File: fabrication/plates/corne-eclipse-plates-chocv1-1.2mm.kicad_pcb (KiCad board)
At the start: 2 copper layers, 272.4 x 180.5 mm, 46 parts

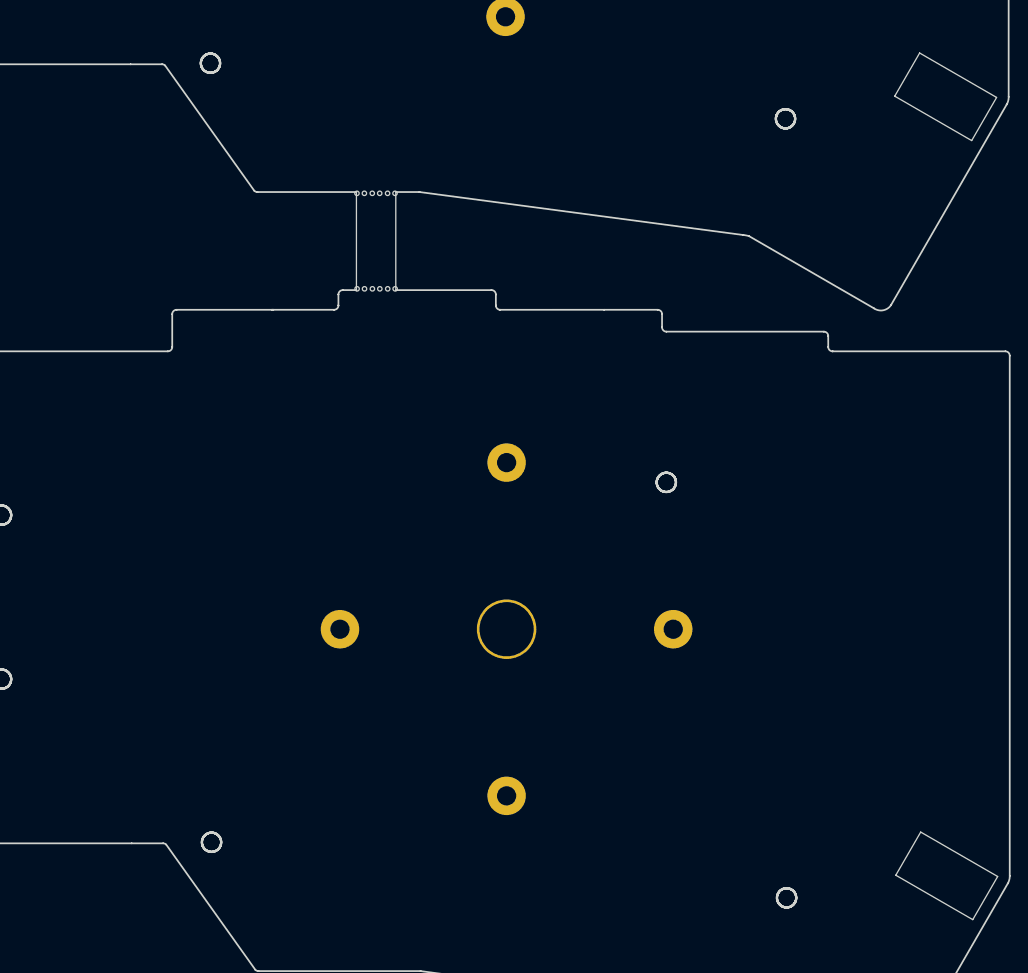
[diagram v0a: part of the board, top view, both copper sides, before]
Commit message: wip: silkscreen, QR codes, plate renames, LED34 cleanup
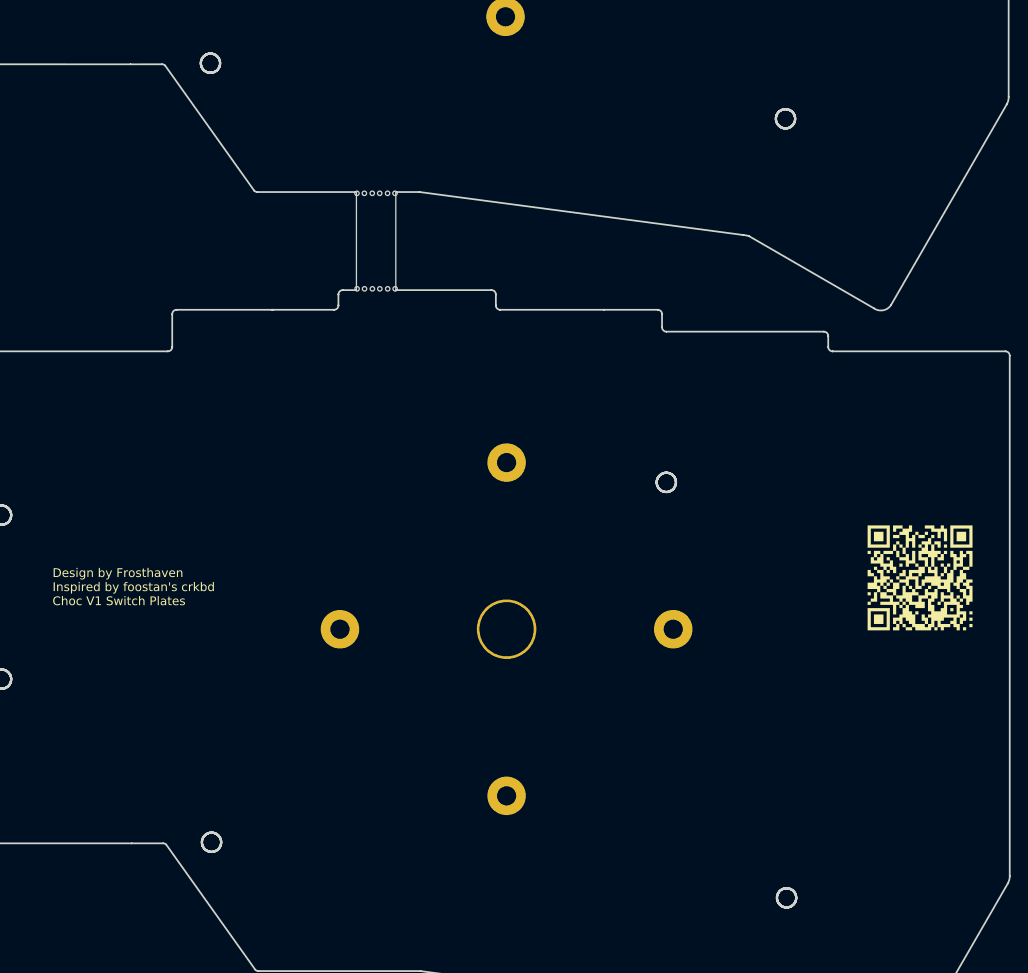
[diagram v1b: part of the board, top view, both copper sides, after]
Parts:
- removed the REF** at (276.5, 174.6)
- removed the REF** at (276.3, 85.6)
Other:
- board text added: "Design by Frosthaven Inspired by foostan's crkbd Choc V1 Switch Plates"

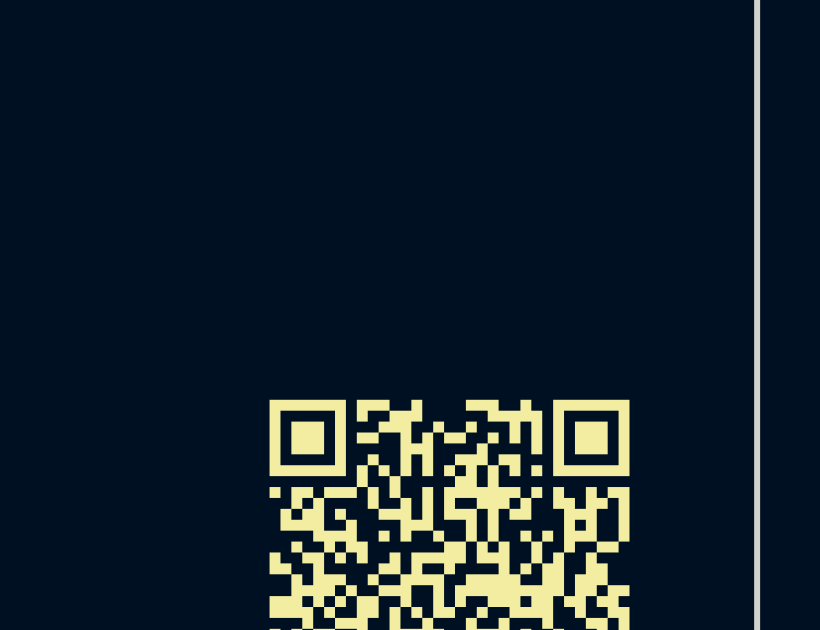
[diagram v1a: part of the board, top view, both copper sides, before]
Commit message: wip: logos, silkscreen cleanup, choc shield STLs, diode alignment
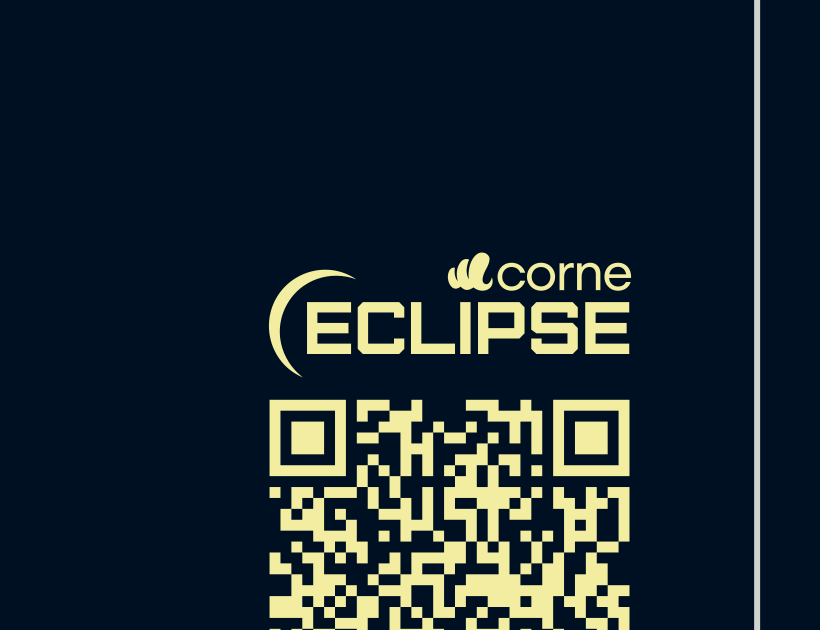
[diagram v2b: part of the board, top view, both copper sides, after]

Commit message: wip
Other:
- outline, holes or cut-outs redrawn

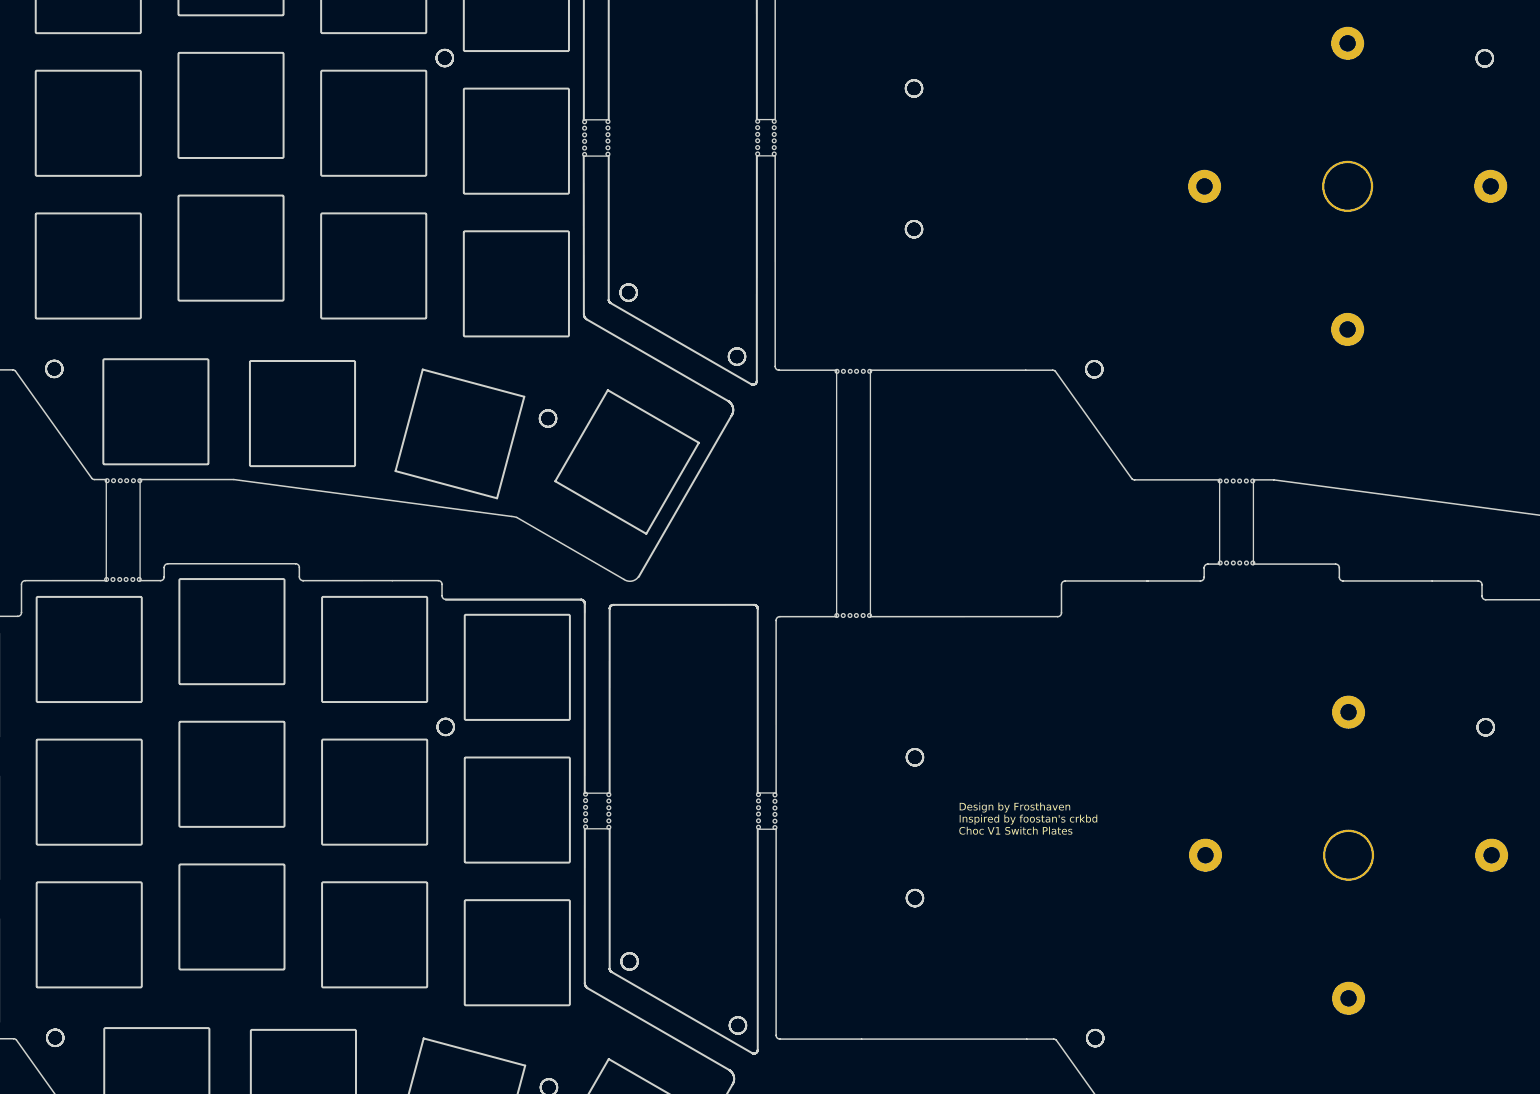
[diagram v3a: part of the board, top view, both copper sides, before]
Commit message: fix(pcbs): aligned screw holes on lp and mx
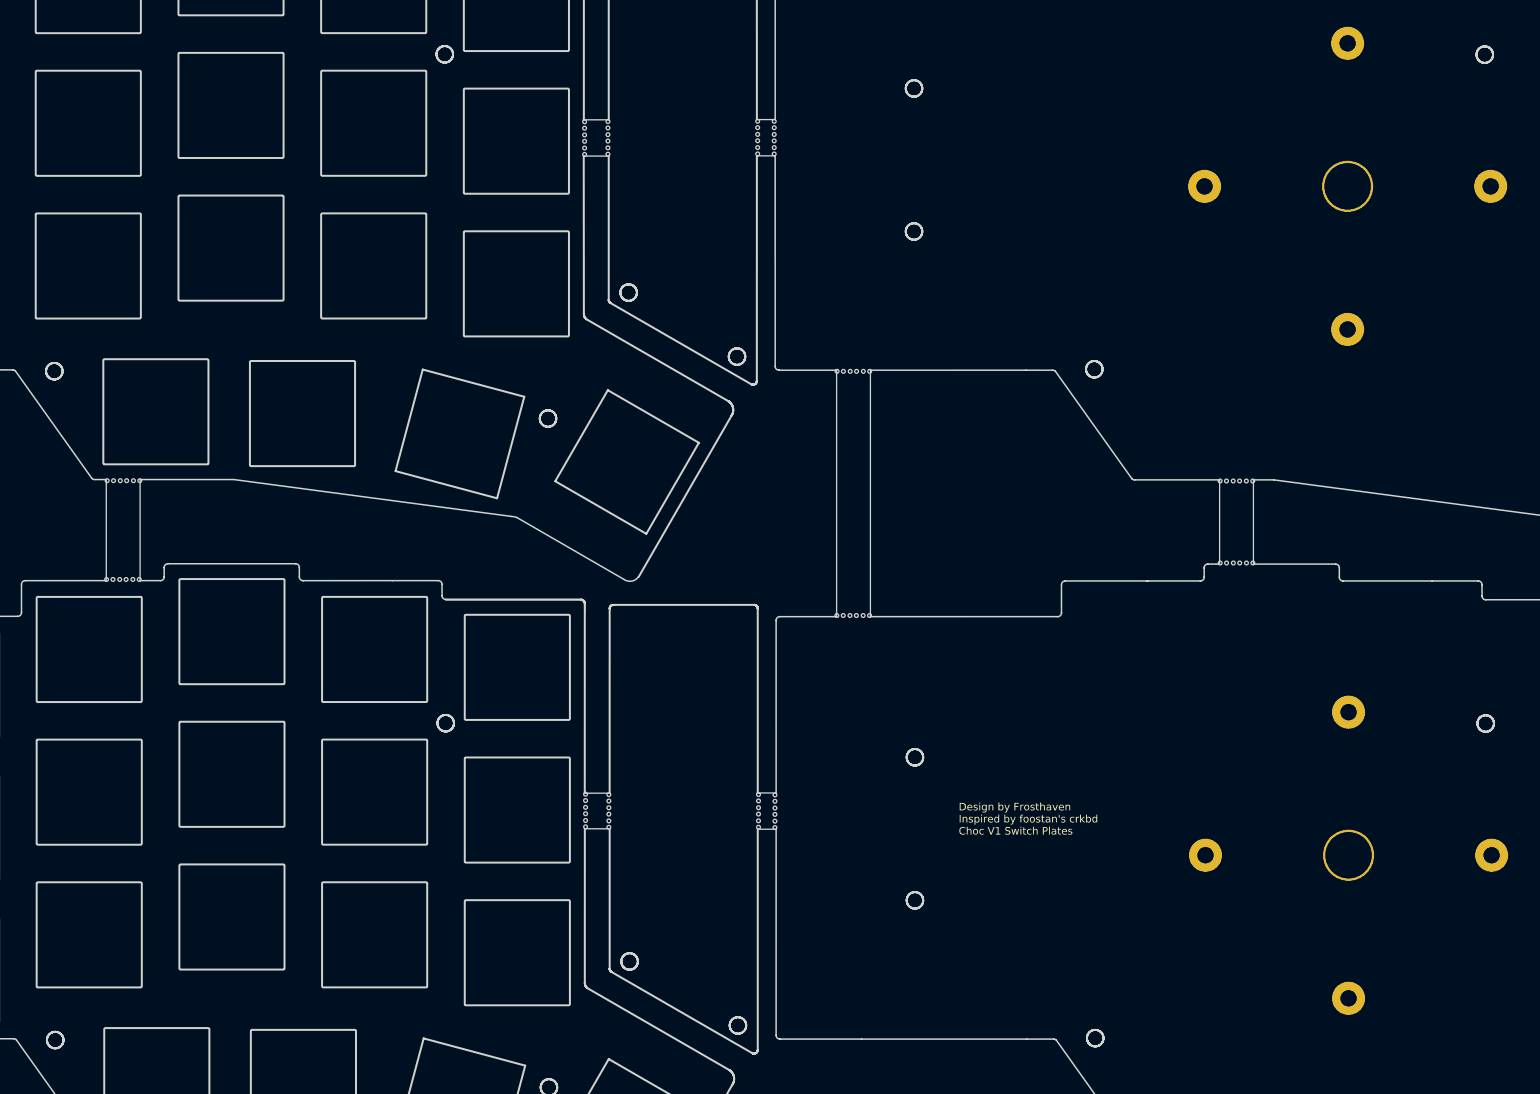
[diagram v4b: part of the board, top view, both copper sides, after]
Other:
- outline, holes or cut-outs redrawn

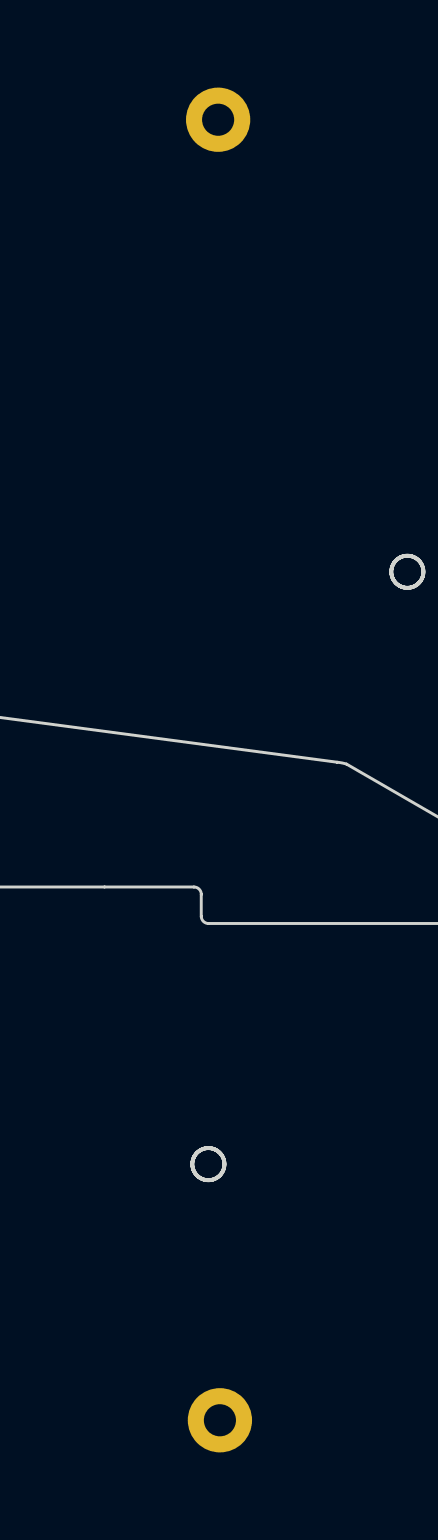
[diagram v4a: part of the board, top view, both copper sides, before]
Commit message: wip(pcbs): choc layout done, mx layout started
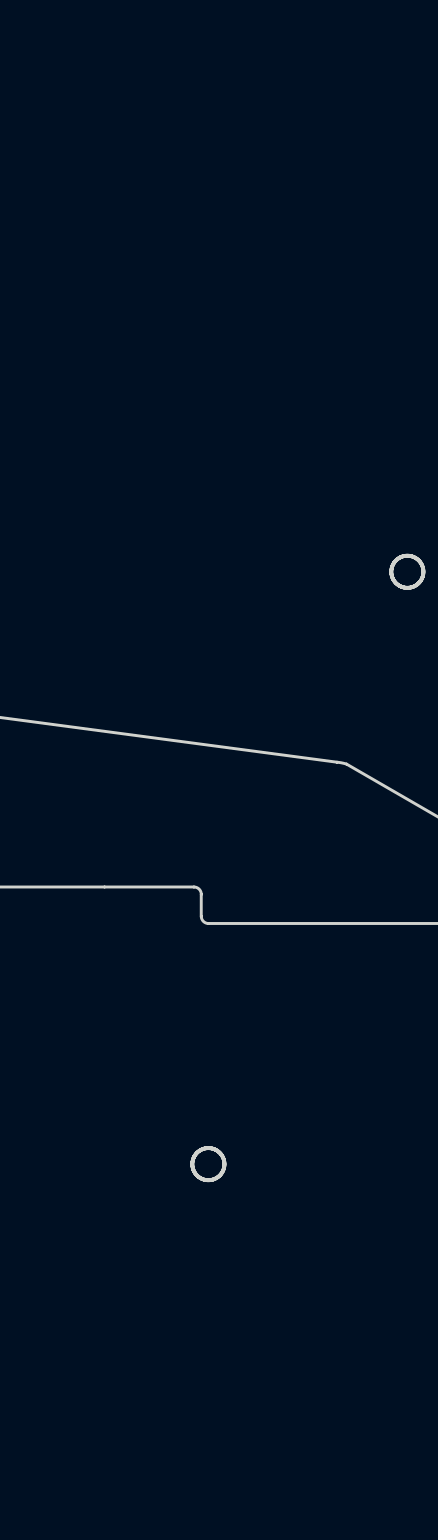
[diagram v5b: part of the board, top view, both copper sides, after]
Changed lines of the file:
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@@
 			(remove_unused_layers no)
 		)
-		(pad "1" thru_hole circle
-			(at 19.05 0)
-			(size 4.4 4.4)
-			(drill 2.2)
-			(layers "*.Cu" "*.Mask")
-			(remove_unused_layers no)
-		)
-		(embedded_fonts no)
+				(embedded_fonts no)
 	)
 	(footprint "Panelization:BreakLine_2h_D0.5mm_P0.85mm"
@@
 			(remove_unused_layers no)
 		)
-		(pad "1" thru_hole circle
-			(at 19.05 0)
-			(size 4.4 4.4)
-			(drill 2.2)
-			(layers "*.Cu" "*.Mask")
-			(remove_unused_layers no)
-		)
-		(embedded_fonts no)
+				(embedded_fonts no)
 	)
 	(gr_poly
